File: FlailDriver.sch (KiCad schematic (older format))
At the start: 92 parts, among them J1 PWR, J2 ROUT, J3 LOUT, J4 GAIN_SEL, J6 AudioJack3_SwitchTR, Q2 MMBT3904, Q4 MMBT3904, Q5 MMBT3904, SW1 PWR, SW3 PWR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

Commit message: commit before routing traces
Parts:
- removed Q2, Q4: MMBT3904, Package_TO_SOT_SMD:SOT-23, symbol Transistor_BJT:MMBT3904
- removed R20, R23: 100k, Resistor_SMD:R_0603_1608Metric_Pad1.05x0.95mm_HandSolder_SmallRef, symbol Device:R
- removed RV3: CTRL3, Crossley_Footprints:SMD_TRIM_JLC_Name, symbol Device:R_POT_TRIM
- removed RV4: VOL, Crossley_Footprints:SMD_TRIM_JLC_Name, symbol Device:R_POT_TRIM
- removed SW6, SW7: SW_Push, HammerheadAudio:JLC_TactileSw_C318884, symbol Switch:SW_Push
- C1, C10, C11, C12, C13, C16, C2, C3, C4, C5, C6, C7, C8, C9: footprint Capacitor_SMD:C_0603_1608Metric_Pad1.05x0.95mm_HandSolder_SmallRef_Top -> Capacitor_SMD:C_0603_1608Metric_Pad1.05x0.95mm_HandSolder_HiddenRef
- C14, C15, C17, C18, C19, C20, C21, C22, C23, C24, C25, C26, C27, C28, C30, C31: footprint Capacitor_SMD:C_0603_1608Metric_Pad1.05x0.95mm_HandSolder_SmallRef -> Capacitor_SMD:C_0603_1608Metric_Pad1.05x0.95mm_HandSolder_HiddenRef
- R1, R10, R11, R12, R13, R14, R15, R17, R18, R19, R2, R21, R22, R25, R26, R3, R4, R5, R6, R8, R9: footprint Resistor_SMD:R_0603_1608Metric_Pad1.05x0.95mm_HandSolder_SmallRef -> Resistor_SMD:R_0603_1608Metric_Pad1.05x0.95mm_HandSolder_HiddenRef
- R7: footprint Resistor_SMD:R_0603_1608Metric_Pad1.05x0.95mm_HandSolder_SmallRef_Top -> Resistor_SMD:R_0603_1608Metric_Pad1.05x0.95mm_HandSolder_HiddenRef
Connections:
- net VCC: now also D2.2 (A); no longer R17.1
- net at R26.2, U6.2 (SDZ), U6.3 (FAULT): now also R17.2
- net at D2.1 (K): now also R17.1
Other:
- moved on the sheet: D2, R17

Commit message: layout progress
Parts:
- added D3, D4: FAULT, LED_SMD:LED_0805_2012Metric_Pad1.15x1.40mm_HandSolder, symbol Device:LED
- added R16, R20: 2.2k, Resistor_SMD:R_0603_1608Metric_Pad1.05x0.95mm_HandSolder_HiddenRef, symbol Device:R
- added RV3: VOL, Crossley_Footprints:SMD_TRIM_JLC, symbol Device:R_POT_TRIM
- H1, H2, H3, H4: footprint HammerheadAudio:M3_MOUNT_KEEPOUT_2 -> HammerheadAudio:M3_Plated; symbol Mechanical:MountingHole -> Mechanical:MountingHole_Pad
- RV1, RV2, RV5, RV6: footprint Crossley_Footprints:SMD_TRIM_JLC_Name -> Crossley_Footprints:SMD_TRIM_JLC
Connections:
- net +3V3: now also RV3.3
- net GND: now also H1.1, H2.1, H3.1, H4.1, D3.1 (K), D4.1 (K), RV3.1
- net VOL: now also RV3.2
- net at U4.10 (8_PWM): now also R16.1
- net at U4.11 (9_PWM): now also R20.2
- new net: D4.2 (A), R20.1
- new net: D3.2 (A), R16.2
- no-connect marks 32 -> 30
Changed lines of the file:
@@
 F 0 "RV5" V 2443 3450 50  0000 C CNN
 F 1 "TRIM_R" V 2534 3450 50  0000 C CNN
-F 2 "Crossley_Footprints:SMD_TRIM_JLC_Name" H 2650 3450 50  0001 C CNN
+F 2 "Crossley_Footprints:SMD_TRIM_JLC" H 2650 3450 50  0001 C CNN
 F 3 "~" H 2650 3450 50  0001 C CNN
 F 4 "C128550" H 2650 3450 50  0001 C CNN "LCSC"
@@
 F 0 "RV6" V 2443 5000 50  0000 C CNN
 F 1 "TRIM_L" V 2534 5000 50  0000 C CNN
-F 2 "Crossley_Footprints:SMD_TRIM_JLC_Name" H 2650 5000 50  0001 C CNN
+F 2 "Crossley_Footprints:SMD_TRIM_JLC" H 2650 5000 50  0001 C CNN
 F 3 "~" H 2650 5000 50  0001 C CNN
 F 4 "C128550" H 2650 5000 50  0001 C CNN "LCSC"
@@
 $EndComp
 $Comp
-L Mechanical:MountingHole H2
+L Mechanical:MountingHole_Pad H2
 U 1 1 6341E6CC
 P 9200 6950
 F 0 "H2" H 9300 6996 50  0000 L CNN
 F 1 "MountingHole" H 9300 6905 50  0000 L CNN
-F 2 "HammerheadAudio:M3_MOUNT_KEEPOUT_2" H 9200 6950 50  0001 C CNN
+F 2 "HammerheadAudio:M3_Plated" H 9200 6950 50  0001 C CNN
 F 3 "~" H 9200 6950 50  0001 C CNN
 	1    9200 6950
@@
 $EndComp
 $Comp
-L Mechanical:MountingHole H3
+L Mechanical:MountingHole_Pad H3
 U 1 1 6341E6CD
 P 9950 6950
 F 0 "H3" H 10050 6996 50  0000 L CNN
 F 1 "MountingHole" H 10050 6905 50  0000 L CNN
-F 2 "HammerheadAudio:M3_MOUNT_KEEPOUT_2" H 9950 6950 50  0001 C CNN
+F 2 "HammerheadAudio:M3_Plated" H 9950 6950 50  0001 C CNN
 F 3 "~" H 9950 6950 50  0001 C CNN
 	1    9950 6950
@@
 $EndComp
 $Comp
-L Mechanical:MountingHole H4
+L Mechanical:MountingHole_Pad H4
 U 1 1 63188933
 P 10700 6950
 F 0 "H4" H 10800 6996 50  0000 L CNN
 F 1 "MountingHole" H 10800 6905 50  0000 L CNN
-F 2 "HammerheadAudio:M3_MOUNT_KEEPOUT_2" H 10700 6950 50  0001 C CNN
+F 2 "HammerheadAudio:M3_Plated" H 10700 6950 50  0001 C CNN
 F 3 "~" H 10700 6950 50  0001 C CNN
 	1    10700 6950
@@
 $EndComp
 $Comp
-L Mechanical:MountingHole H1
+L Mechanical:MountingHole_Pad H1
 U 1 1 6341E6CE
 P 8450 6950
 F 0 "H1" H 8550 6996 50  0000 L CNN
 F 1 "MountingHole" H 8550 6905 50  0000 L CNN
-F 2 "HammerheadAudio:M3_MOUNT_KEEPOUT_2" H 8450 6950 50  0001 C CNN
+F 2 "HammerheadAudio:M3_Plated" H 8450 6950 50  0001 C CNN
 F 3 "~" H 8450 6950 50  0001 C CNN
 	1    8450 6950
@@
 F 0 "RV1" V 6593 9950 50  0000 C CNN
 F 1 "CTRL1" V 6684 9950 50  0000 C CNN
-F 2 "Crossley_Footprints:SMD_TRIM_JLC_Name" H 6800 9950 50  0001 C CNN
+F 2 "Crossley_Footprints:SMD_TRIM_JLC" H 6800 9950 50  0001 C CNN
 F 3 "~" H 6800 9950 50  0001 C CNN
 F 4 "C128550" H 6800 9950 50  0001 C CNN "LCSC"
@@
 F 0 "RV2" V 6593 10800 50  0000 C CNN
 F 1 "CTRL2" V 6684 10800 50  0000 C CNN
-F 2 "Crossley_Footprints:SMD_TRIM_JLC_Name" H 6800 10800 50  0001 C CNN
+F 2 "Crossley_Footprints:SMD_TRIM_JLC" H 6800 10800 50  0001 C CNN
 F 3 "~" H 6800 10800 50  0001 C CNN
 F 4 "C128550" H 6800 10800 50  0001 C CNN "LCSC"
@@
 Wire Wire Line
 	1650 9700 1700 9700
-Wire Wire Line
-	1700 9900 1650 9900
-Wire Wire Line
-	1700 10000 1650 10000
 Wire Wire Line
 	1700 10100 1650 10100
@@
 Text GLabel 1650 9600 0    50   Input ~ 0
 BT4
-NoConn ~ 1650 9900
-NoConn ~ 1650 10000
 NoConn ~ 1650 10100
 NoConn ~ 1650 10200
@@
 Wire Wire Line
 	7450 2750 7850 2750
+$Comp
+L Device:LED D4
+U 1 1 67295746
+P 200 10500
+F 0 "D4" V 239 10382 50  0000 R CNN
+F 1 "FAULT" V 148 10382 50  0000 R CNN
+F 2 "LED_SMD:LED_0805_2012Metric_Pad1.15x1.40mm_HandSolder" H 200 10500 50  0001 C CNN
+F 3 "C84256" H 200 10500 50  0001 C CNN
+F 4 "C84256" H 200 10500 50  0001 C CNN "LCSC"
+	1    200  10500
+	1    0    0    1
+$EndComp
+$Comp
+L Device:R R20
+U 1 1 672BA9E2
+P 550 10500
+F 0 "R20" H 620 10546 50  0000 L CNN
+F 1 "2.2k" H 620 10455 50  0000 L CNN
+F 2 "Resistor_SMD:R_0603_1608Metric_Pad1.05x0.95mm_HandSolder_HiddenRef" V 480 10500 50  0001 C CNN
+F 3 "C4190" H 550 10500 50  0001 C CNN
+F 4 "C4190" H 550 10500 50  0001 C CNN "LCSC"
+	1    550  10500
+	0    -1   1    0
+$EndComp
+$Comp
+L Device:LED D3
+U 1 1 672DFDBA
+P 200 10050
+F 0 "D3" V 239 9932 50  0000 R CNN
+F 1 "FAULT" V 148 9932 50  0000 R CNN
+F 2 "LED_SMD:LED_0805_2012Metric_Pad1.15x1.40mm_HandSolder" H 200 10050 50  0001 C CNN
+F 3 "C84256" H 200 10050 50  0001 C CNN
+F 4 "C84256" H 200 10050 50  0001 C CNN "LCSC"
+	1    200  10050
+	1    0    0    1
+$EndComp
+$Comp
+L Device:R R16
+U 1 1 672DFDC5
+P 550 10050
+F 0 "R16" H 620 10096 50  0000 L CNN
+F 1 "2.2k" H 620 10005 50  0000 L CNN
+F 2 "Resistor_SMD:R_0603_1608Metric_Pad1.05x0.95mm_HandSolder_HiddenRef" V 480 10050 50  0001 C CNN
+F 3 "C4190" H 550 10050 50  0001 C CNN
+F 4 "C4190" H 550 10050 50  0001 C CNN "LCSC"
+	1    550  10050
+	0    1    -1   0
+$EndComp
+Wire Wire Line
+	800  9900 800  10050
+Wire Wire Line
+	800  10050 700  10050
+Wire Wire Line
+	800  9900 1700 9900
+Wire Wire Line
+	350  10050 400  10050
+Wire Wire Line
+	350  10500 400  10500
+Wire Wire Line
+	700  10500 900  10500
+Wire Wire Line
+	900  10500 900  10000
+Wire Wire Line
+	900  10000 1700 10000
+$Comp
+L power:GND #PWR0109
+U 1 1 6747DCA8
+P -50 10600
+F 0 "#PWR0109" H -50 10350 50  0001 C CNN
+F 1 "GND" H -45 10427 50  0000 C CNN
+F 2 "" H -50 10600 50  0001 C CNN
+F 3 "" H -50 10600 50  0001 C CNN
+	1    -50  10600
+	1    0    0    -1
+$EndComp
+Wire Wire Line
+	-50  10600 -50  10500
+Wire Wire Line
+	-50  10050 50   10050
+Wire Wire Line
+	-50  10500 50   10500
+Connection ~ -50  10500
+Wire Wire Line
+	-50  10500 -50  10050
+$Comp
+L power:+3.3V #PWR0132
+U 1 1 674D4646
+P 8200 9950
+F 0 "#PWR0132" H 8200 9800 50  0001 C CNN
+F 1 "+3.3V" H 8215 10123 50  0000 C CNN
+F 2 "" H 8200 9950 50  0001 C CNN
+F 3 "" H 8200 9950 50  0001 C CNN
+	1    8200 9950
+	0    1    1    0
+$EndComp
+$Comp
+L power:GND #PWR0138
+U 1 1 674D4650
+P 7800 9950
+F 0 "#PWR0138" H 7800 9700 50  0001 C CNN
+F 1 "GND" H 7805 9777 50  0000 C CNN
+F 2 "" H 7800 9950 50  0001 C CNN
+F 3 "" H 7800 9950 50  0001 C CNN
+	1    7800 9950
+	0    1    1    0
+$EndComp
+Wire Wire Line
+	7800 9950 7850 9950
+Wire Wire Line
+	8150 9950 8200 9950
+Wire Wire Line
+	8000 10100 8000 10150
+$Comp
+L Device:R_POT_TRIM RV3
+U 1 1 674D465F
+P 8000 9950
+F 0 "RV3" V 7793 9950 50  0000 C CNN
+F 1 "VOL" V 7884 9950 50  0000 C CNN
+F 2 "Crossley_Footprints:SMD_TRIM_JLC" H 8000 9950 50  0001 C CNN
+F 3 "~" H 8000 9950 50  0001 C CNN
+F 4 "C128550" H 8000 9950 50  0001 C CNN "LCSC"
+	1    8000 9950
+	0    -1   1    0
+$EndComp
+Text GLabel 8000 10150 3    50   Input ~ 0
+VOL
+$Comp
+L power:GND #PWR0139
+U 1 1 6750685A
+P 8450 7150
+F 0 "#PWR0139" H 8450 6900 50  0001 C CNN
+F 1 "GND" H 8455 6977 50  0000 C CNN
+F 2 "" H 8450 7150 50  0001 C CNN
+F 3 "" H 8450 7150 50  0001 C CNN
+	1    8450 7150
+	1    0    0    -1
+$EndComp
+Wire Wire Line
+	8450 7050 8450 7100
+Wire Wire Line
+	8450 7100 9200 7100
+Wire Wire Line
+	10700 7100 10700 7050
+Connection ~ 8450 7100
+Wire Wire Line
+	8450 7100 8450 7150
+Wire Wire Line
+	9950 7100 9950 7050
+Connection ~ 9950 7100
+Wire Wire Line
+	9950 7100 10700 7100
+Wire Wire Line
+	9200 7100 9200 7050
+Connection ~ 9200 7100
+Wire Wire Line
+	9200 7100 9950 7100
 $EndSCHEMATC

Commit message: layout progress
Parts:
- removed J6: AudioJack3_SwitchTR, Connectors:AUDIO-JACK, symbol Connector:AudioJack3_SwitchTR
- removed SW3: PWR, HammerheadAudio:JLC_SW_SPDT_SMT_C145845, symbol Switch:SW_SPDT
- added J5: LEFT, HammerheadAudio:EuroJack_MonoSW_THT_NOREF_SmallHoles_NoSilk, symbol Connector:EuroJack_Mono_3.5mm_Switched
- added J6: RIGHT, HammerheadAudio:EuroJack_MonoSW_THT_NOREF_SmallHoles_NoSilk, symbol Connector:EuroJack_Mono_3.5mm_Switched
- added SW3: SW_Push, HammerheadAudio:JLC_TactileSw_C318884, symbol Switch:SW_Push
- D4: value FAULT -> IND
- J2: value ROUT -> LOUT
- J3: value LOUT -> ROUT
- U4: footprint MeowWolf_Templates:TEENSY_3.5_3.6_MINIMAL -> MeowWolf_Templates:TEENSY_4.1_MINIMAL_DROP_IN
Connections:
- net BT3 is gone; now on net BT2: U4.6 (4_PWM)
- net CTRL3 is gone; now on net CTRL2: U4.39 (17_A3)
- net AL: now also J5.3
- net AR: now also J6.3
- net BT1: now also U4.5 (3_PWM); no longer U4.4 (2_PWM)
- net BT2: no longer U4.5 (3_PWM)
- net CTRL1: now also U4.38 (16_A2); no longer U4.37 (15_PWM_A1)
- net CTRL2: no longer U4.38 (16_A2)
- net GND: now also J5.2, J6.2, SW3.1
- net LIN: now also J5.1
- net LIN+: now also C11.1, U6.4 (RIN+); no longer C9.1, U6.10 (LIN+)
- net LIN-: now also C12.1, U6.5 (RIN-); no longer C10.1, U6.11 (LIN-)
- net MUTE_IN: now also U4.37 (15_PWM_A1), SW3.2; no longer U4.8 (6_PWM)
- net RIN: now also J6.1
- net RIN+: now also C9.1, U6.10 (LIN+); no longer C11.1, U6.4 (RIN+)
- net RIN-: now also C10.1, U6.11 (LIN-); no longer C12.1, U6.5 (RIN-)
- net UNMUTE: now also U4.36 (14_PWM_A0); no longer U4.2 (0_PWM)
- net VCC: now also SW1.1 (A); no longer SW1.3 (C)
- net at U4.10 (8_PWM): now also R20.2; no longer R16.1
- net at U4.11 (9_PWM): now also R16.1; no longer R20.2
- net at U3.1, U3.2 (-): now also RV6.3; no longer C11.2
- net at C1.1, R3.2, R4.1: now also U3.3 (+); no longer U2.3 (+)
- net at C2.1, R5.2, R6.1: now also U2.3 (+); no longer U2.5 (+)
- net at U2.6 (-), U2.7: now also C11.2; no longer RV6.3
- net at RV5.2: now also U2.5 (+); no longer U3.3 (+)
- net BT4: no longer names the net of U4.7 (5_PWM)
- net FAULT: no longer names the net of U4.3 (1_PWM)
- no-connect marks 30 -> 32
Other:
- moved on the sheet: C10, C11, C12, C4, C5, C9, D3, D4, R16, R20, RV5, RV6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

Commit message: layout finished
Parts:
- J1, J2, J3: footprint HammerheadAudio:Phoenix_Stacked_Marking2_NoRef_Centered_BoardEdge -> HammerheadAudio:Phoenix_Stacked_BackSilk_Centered_BoardEdge
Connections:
- net BT1: now also U4.14 (12_PWM); no longer U4.5 (3_PWM)
- net BT2: now also U4.13 (11_PWM); no longer U4.6 (4_PWM)
- net CTRL1: now also U4.39 (17_A3); no longer U4.38 (16_A2)
- net CTRL2: now also U4.40 (18_PWM_A4); no longer U4.39 (17_A3)
- net VOL: now also U4.38 (16_A2); no longer U4.40 (18_PWM_A4)
- no-connect marks 32 -> 33
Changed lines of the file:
@@
 	1650 9000 1700 9000
 Wire Wire Line
-	4000 10200 3950 10200
-Wire Wire Line
-	1650 9400 1700 9400
-Wire Wire Line
-	1650 9500 1700 9500
+	1650 10200 1700 10200
+Wire Wire Line
+	1650 10300 1700 10300
 Wire Wire Line
 	1650 9100 1700 9100
@@
 Wire Wire Line
 	3950 10600 4000 10600
-Text GLabel 4000 9900 2    50   Input ~ 0
-CTRL2
 Wire Wire Line
 	3950 10400 4300 10400
-Text GLabel 4000 9800 2    50   Input ~ 0
-VOL
 Wire Wire Line
 	3950 10500 4000 10500
@@
 Wire Wire Line
 	7200 1050 7300 1050
-Text GLabel 4000 10200 2    50   Input ~ 0
-UNMUTE
 Wire Wire Line
 	9950 2750 10050 2750
@@
 Text GLabel 4000 10100 2    50   Input ~ 0
 MUTE_IN
-Text GLabel 4000 10000 2    50   Input ~ 0
-CTRL1
 Text GLabel 1650 9800 0    50   Input ~ 0
 DIN
@@
 F 0 "J1" H 1118 875 50  0000 C CNN
 F 1 "PWR" H 1118 966 50  0000 C CNN
-F 2 "HammerheadAudio:Phoenix_Stacked_Marking2_NoRef_Centered_BoardEdge" H 1200 1200 50  0001 C CNN
+F 2 "HammerheadAudio:Phoenix_Stacked_BackSilk_Centered_BoardEdge" H 1200 1200 50  0001 C CNN
 F 3 "~" H 1200 1200 50  0001 C CNN
 F 4 "C430323" H 1200 1200 50  0001 C CNN "LCSC"
@@
 F 0 "J2" H 11168 2775 50  0000 C CNN
 F 1 "LOUT" H 11168 2866 50  0000 C CNN
-F 2 "HammerheadAudio:Phoenix_Stacked_Marking2_NoRef_Centered_BoardEdge" H 11250 3100 50  0001 C CNN
+F 2 "HammerheadAudio:Phoenix_Stacked_BackSilk_Centered_BoardEdge" H 11250 3100 50  0001 C CNN
 F 3 "~" H 11250 3100 50  0001 C CNN
 F 4 "C430323" H 11250 3100 50  0001 C CNN "LCSC"
@@
 F 0 "J3" H 11168 4025 50  0000 C CNN
 F 1 "ROUT" H 11168 4116 50  0000 C CNN
-F 2 "HammerheadAudio:Phoenix_Stacked_Marking2_NoRef_Centered_BoardEdge" H 11250 4350 50  0001 C CNN
+F 2 "HammerheadAudio:Phoenix_Stacked_BackSilk_Centered_BoardEdge" H 11250 4350 50  0001 C CNN
 F 3 "~" H 11250 4350 50  0001 C CNN
 F 4 "C430323" H 11250 4350 50  0001 C CNN "LCSC"
@@
 Wire Wire Line
 	3950 9900 4000 9900
-Text GLabel 1650 9400 0    50   Input ~ 0
+Text GLabel 1650 10300 0    50   Input ~ 0
 BT1
-Text GLabel 1650 9500 0    50   Input ~ 0
+Text GLabel 1650 10200 0    50   Input ~ 0
 BT2
 NoConn ~ 1650 9200
@@
 	1700 10100 1650 10100
 Wire Wire Line
-	1700 10200 1650 10200
-Wire Wire Line
-	1700 10300 1650 10300
+	1700 9400 1650 9400
+Wire Wire Line
+	1700 9500 1650 9500
 NoConn ~ 1650 10100
-NoConn ~ 1650 10200
-NoConn ~ 1650 10300
+NoConn ~ 1650 9400
+NoConn ~ 1650 9500
 $Comp
 L Device:LED D3
@@
 	1    0    0    1
 $EndComp
+Text GLabel 4000 9900 2    50   Input ~ 0
+CTRL1
+Text GLabel 4000 9800 2    50   Input ~ 0
+CTRL2
+Wire Wire Line
+	4000 10200 3950 10200
+Text GLabel 4000 10200 2    50   Input ~ 0
+UNMUTE
+Text GLabel 4000 10000 2    50   Input ~ 0
+VOL
+Wire Wire Line
+	1700 9600 1650 9600
+NoConn ~ 1650 9600
 $EndSCHEMATC

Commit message: bak
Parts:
- C15: LCSC C15849 -> C15849
- R16, R20: value 2.2k -> 100; LCSC C4190 -> C22775

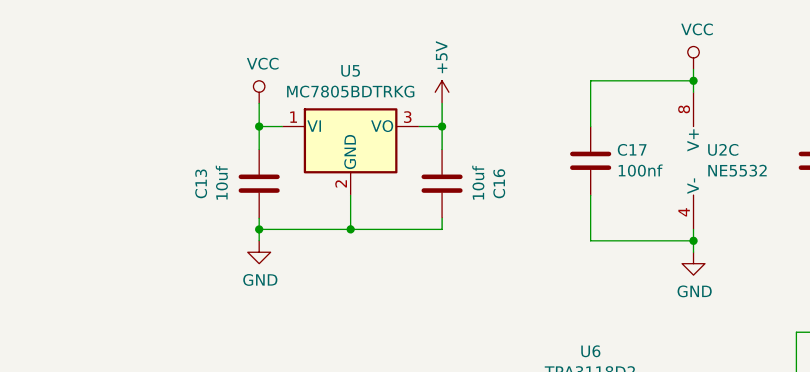
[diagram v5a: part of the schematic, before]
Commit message: switching 5V regulator
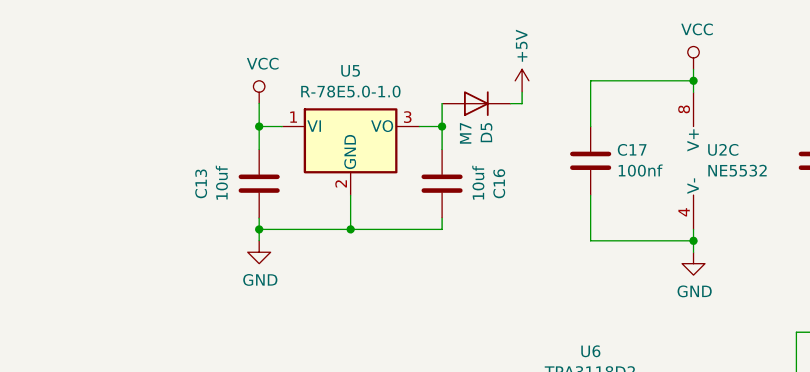
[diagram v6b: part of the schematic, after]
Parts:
- added D5: M7, Diode_SMD:D_SMA, symbol Device:D
- U5: value MC7805BDTRKG -> R-78E5.0-1.0; footprint Package_TO_SOT_SMD:TO-252-2 -> HammerheadAudio:TRACO_DCDC; LCSC C110908 -> C15077
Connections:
- net +5V: now also D5.1 (K); no longer C16.1, U5.3 (VO)
- new net: C16.1, D5.2 (A), U5.3 (VO)
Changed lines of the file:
@@
 EESchema Schematic File Version 4
-LIBS:AmpClassD_Daugher-cache
-LIBS:BorosDriver-cache
-LIBS:BorosRedress-cache
-LIBS:16OhmSpeaker_Breakout-cache
-LIBS:TeensyCodec_Daughter-cache
-LIBS:TeensyDac8_Breakout-cache
+LIBS:FlailDriver-cache
 EELAYER 29 0
 EELAYER END
@@
 L power:+5V #PWR0148
 U 1 1 64196696
-P 8000 950
-F 0 "#PWR0148" H 8000 800 50  0001 C CNN
-F 1 "+5V" V 8000 1150 50  0000 C CNN
-F 2 "" H 8000 950 50  0001 C CNN
-F 3 "" H 8000 950 50  0001 C CNN
-	1    8000 950
+P 8350 900
+F 0 "#PWR0148" H 8350 750 50  0001 C CNN
+F 1 "+5V" V 8350 1100 50  0000 C CNN
+F 2 "" H 8350 900 50  0001 C CNN
+F 3 "" H 8350 900 50  0001 C CNN
+	1    8350 900
 	1    0    0    -1
 $EndComp
@@
 P 7600 1050
 F 0 "U5" H 7600 1292 50  0000 C CNN
-F 1 "MC7805BDTRKG" H 7600 1201 50  0000 C CNN
-F 2 "Package_TO_SOT_SMD:TO-252-2" H 7600 1275 50  0001 C CIN
-F 3 "C110908" H 7600 1000 50  0001 C CNN
-F 4 "C110908" H 7600 1050 50  0001 C CNN "LCSC"
+F 1 "R-78E5.0-1.0" H 7600 1201 50  0000 C CNN
+F 2 "HammerheadAudio:TRACO_DCDC" H 7600 1275 50  0001 C CIN
+F 3 "C15077" H 7600 1000 50  0001 C CNN
+F 4 "C15077" H 7600 1050 50  0001 C CNN "LCSC"
 	1    7600 1050
 	1    0    0    -1
@@
 	1    0    0    -1
 $EndComp
+$Comp
+L Device:D D5
+U 1 1 64A6F004
+P 8150 950
+F 0 "D5" V 8104 1029 50  0000 L CNN
+F 1 "M7" V 8195 1029 50  0000 L CNN
+F 2 "Diode_SMD:D_SMA" H 8150 950 50  0001 C CNN
+F 3 "C95872" H 8150 950 50  0001 C CNN
+F 4 "C95872" H 8150 950 50  0001 C CNN "LCSC"
+	1    8150 950
+	-1   0    0    1
+$EndComp
+Wire Wire Line
+	8300 950  8350 950
+Wire Wire Line
+	8350 950  8350 900
 $EndSCHEMATC

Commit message: newreg
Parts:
- added SW2: SW_DIP_x02, HammerheadAudio:JLC_SMD_DIP_SPSTx2_C40735, symbol Switch:SW_DIP_x02
- U5: LCSC C15077 -> (none)
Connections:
- net AL: now also SW2.4
- net AR: now also SW2.3
- net LIN: now also SW2.1
- net RIN: now also SW2.2
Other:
- moved on the sheet: C1, C10, C11, C12, C13, C14, C15, C16, C17, C18, C19, C2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
